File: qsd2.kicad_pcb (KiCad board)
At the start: 2 copper layers, 100 x 75 mm, 72 parts, among them J1 5-1814832-1, J2 5-1814832-1, J3 Conn_02x08_Odd_Even, J4 SJ-3524-SMT, J5 B4B-XH-A_LF__SN_, U1 SN74LVC1G14DBV, U10 GALI-39, U11 SN74LVC1G14DBV, U12 LM4040DBZ-2.5, U13 LM4040DBZ-2.5, U2 SN74LVC1G14DBV, U3 SN74CBT3253, U4 SN74AC74PW, U5 AD8226ARZ-R7, U6 AD8226ARZ-R7, U9 UA78M05IDCYR

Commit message: V1.2 to fab.
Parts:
- removed R16: DNP, Resistor_SMD:R_1206_3216Metric
- removed R19: 4.7k, Resistor_SMD:R_1206_3216Metric
- removed U12, U13: LM4040DBZ-2.5, Package_TO_SOT_SMD:SOT-23
- added C26: 1uF, Capacitor_SMD:C_1206_3216Metric, F.Cu at (171.9, 62.4)
- added U7: AP7343, Package_TO_SOT_SMD:SOT-23-5, F.Cu at (176.8, 80.7)
- R18: value 4.7k -> 2.2k
- R23, R24: value 2.61k -> 10k
- moved C27 18.7 mm to (173.0, 81.1), turned to -90 degrees
- moved C23 10.6 mm to (177.3, 86.3)
- moved R18 9.36 mm to (169.8, 81.1)
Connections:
- C23 pad 1: /REF_I -> /5V_FILT
- C27 pad 1: /REF_Q -> /REF_V
- J4 pad 2: Net-(C21-Pad2) -> Net-(C20-Pad2)
- J4 pad 3: Net-(C20-Pad2) -> Net-(C21-Pad2)
- R18 pad 1: /REF_I -> /REF_V
- R18 pad 2: /5V_FILT -> GND
- U5 pad 6: /REF_I -> /REF_V
- U6 pad 6: /REF_Q -> /REF_V
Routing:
- net /REF_V: track 0.00 -> 32.1 mm, vias 0 -> 2
- net /REF_I: track 25.3 -> 0.00 mm, vias 1 -> 0
- net Net-(C20-Pad2): track 35.0 -> 16.8 mm
- net /REF_Q: track 16.9 -> 0.00 mm, vias 1 -> 0
- net GND: track 12.0 -> 19.0 mm, vias 121 -> 124
- net /5V_FILT: track 209.7 -> 215.7 mm
- net Net-(C21-Pad2): track 33.0 -> 30.2 mm
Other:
- board text added: "GND"
- board text added: "I2C"
- board text added: "SCL"
- board text added: "SDA"
- board text added: "V1.2"
- board text removed: "V1.1"

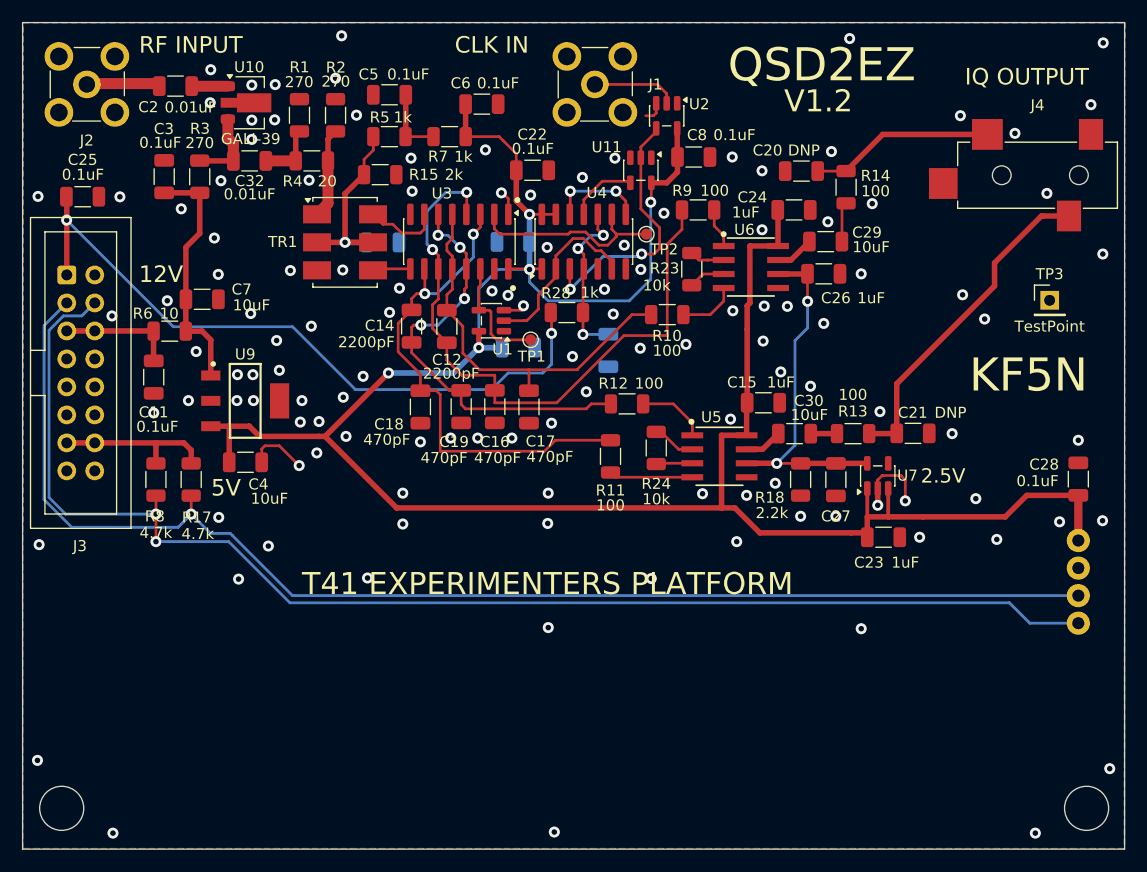
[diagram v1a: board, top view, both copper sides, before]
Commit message: Changed 10 ohm resistor to 20.  Fixed missing component value.
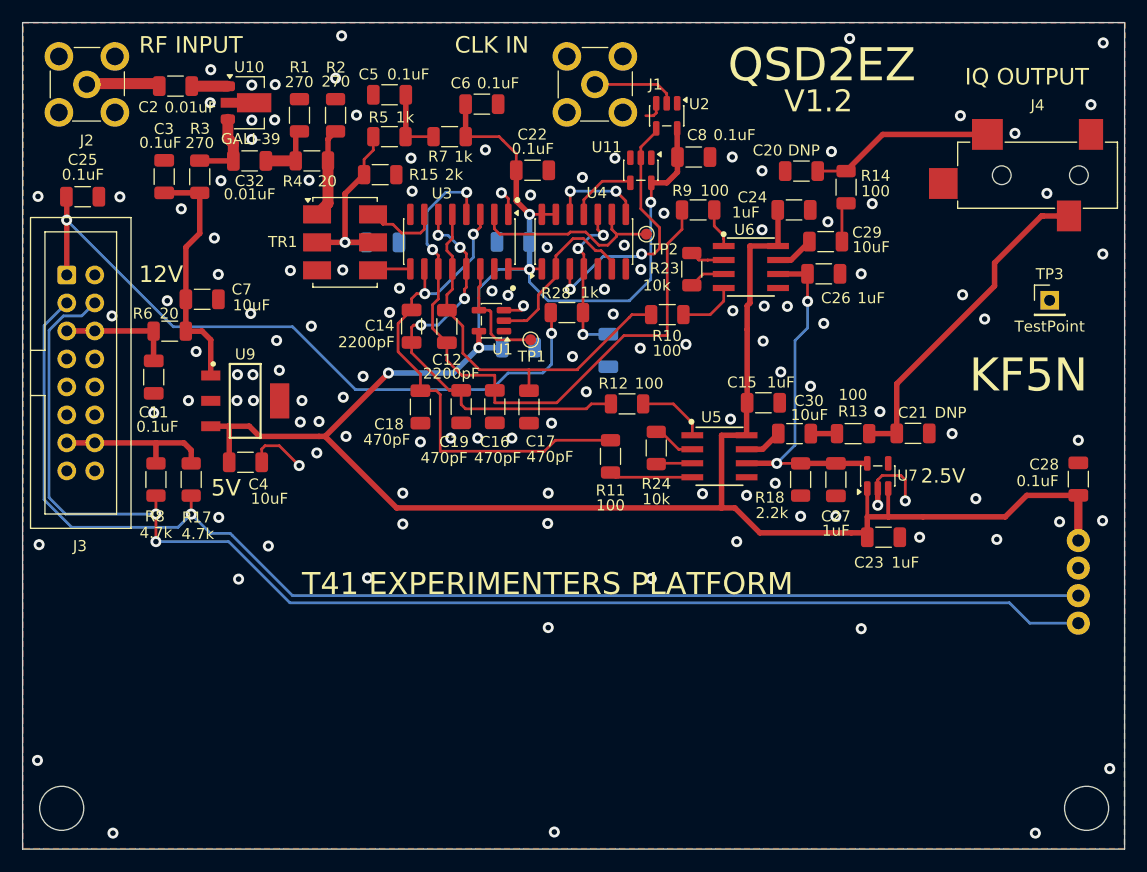
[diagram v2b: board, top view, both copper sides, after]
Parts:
- R6: value 10 -> 20
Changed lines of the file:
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@@
 	(title_block
 		(title "QSD Divide by Two")
-		(date "2026-07-02")
+		(date "2026-07-21")
 		(rev "V1.2")
 	)
@@
 		(property "Value" "1uF"
 			(at 4.625 0 180)
-			(layer "F.Fab")
+			(layer "F.SilkS")
 			(effects
 				(font
@@
 			)
 		)
-		(property "Value" "10"
+		(property "Value" "20"
 			(at -0.05 -1.6 0)
 			(layer "F.SilkS")
@@
 		(tags "resistor")
 		(property "Reference" "R5"
-			(at -0.8875 -1.75 0)
+			(at -0.9875 -1.75 0)
 			(layer "F.SilkS")
 			(effects
@@
 		)
 		(property "Value" "1k"
-			(at 1.2125 -1.75 0)
+			(at 1.4125 -1.75 0)
 			(layer "F.SilkS")
 			(effects

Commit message: Updated PDF schematic.
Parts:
- U4: value SN74AC74PW -> MC74LCX74DR2G
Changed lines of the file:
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@@
 			)
 		)
-		(property "Value" "SN74AC74PW"
+		(property "Value" "MC74LCX74DR2G"
 			(at 0 5.28 90)
 			(layer "F.Fab")
